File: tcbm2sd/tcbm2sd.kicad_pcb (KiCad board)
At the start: 2 copper layers, 56 x 91 mm, 24 parts, among them J1 TCBM, J2 JTAG, J3 GPIO, J4 AMS1117, J5 SD CARD, J6 ALT_A4_A7, J7 ALT_A6_A7, U1 XC9572XL-VQ64, U2 Arduino Pro Mini, U3 AMS1117-3.3

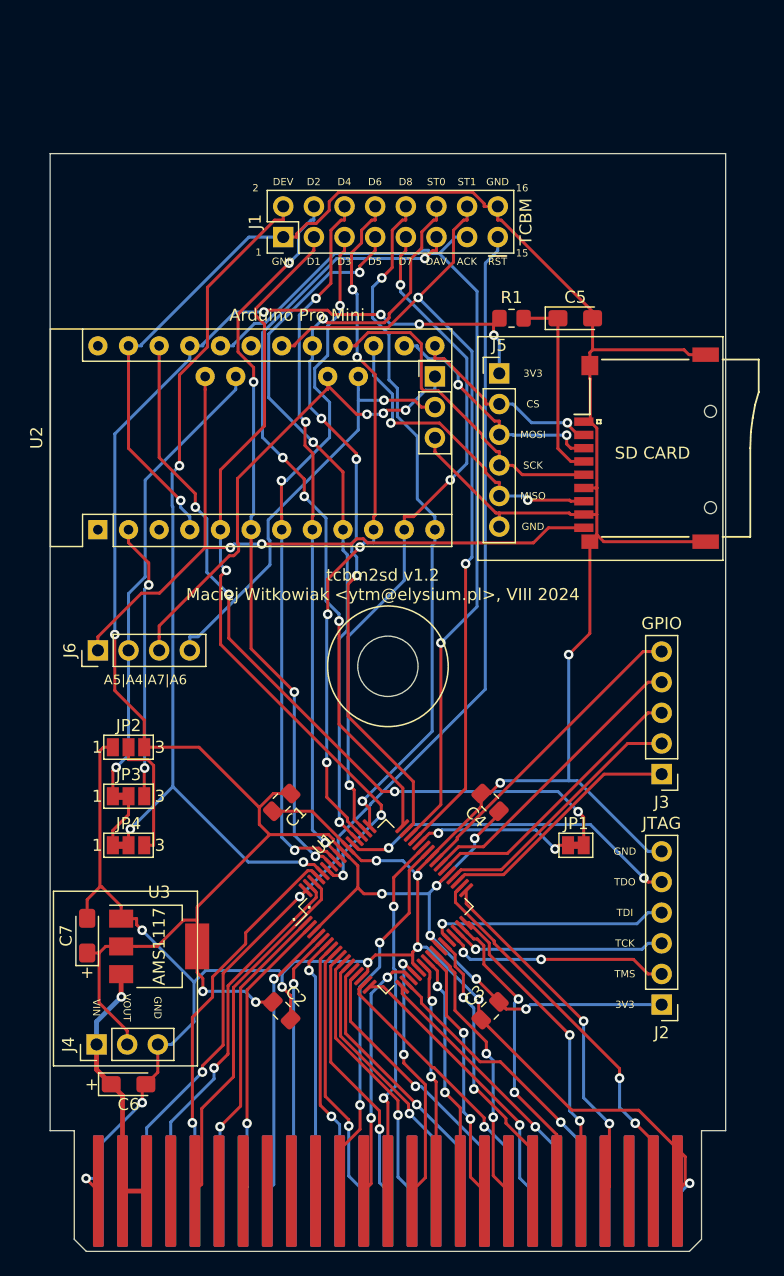
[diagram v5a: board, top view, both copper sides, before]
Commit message: add 32/64K EEPROM with /CS done using two diodes with pullup as AND one more pullup for A15 line connector for remaining Arduino lines with GND connection to short it to disable Arduino on boot
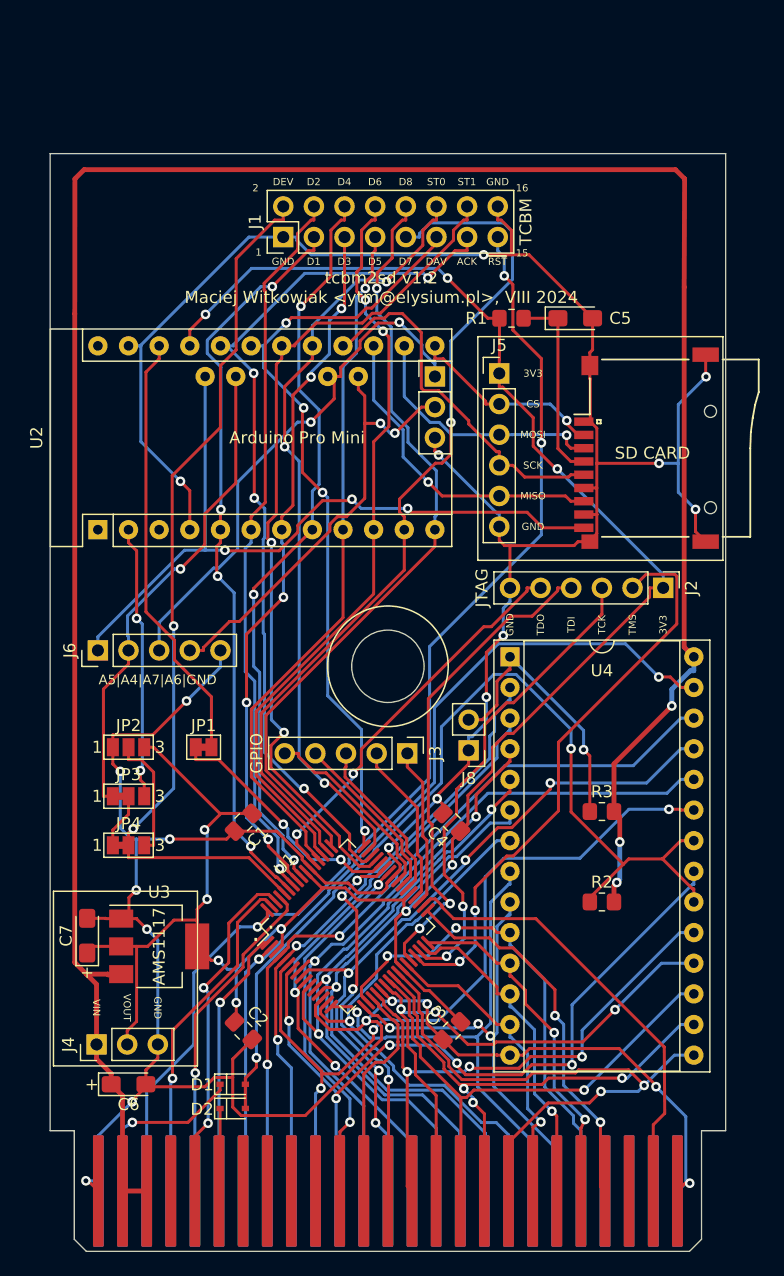
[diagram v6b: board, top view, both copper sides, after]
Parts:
- added D1: 1N4148WS, Diode_SMD:D_SOD-323, F.Cu at (135.6, 136.7)
- added D2: 1N4148WS, Diode_SMD:D_SOD-323, F.Cu at (135.6, 138.7)
- added J8: Conn_01x02, Connector_PinHeader_2.54mm:PinHeader_1x02_P2.54mm_Vertical, F.Cu at (155.2, 109.0)
- added R2: 10K, Resistor_SMD:R_0805_2012Metric_Pad1.20x1.40mm_HandSolder, F.Cu at (166.2, 121.5)
- added R3: 10K, Resistor_SMD:R_0805_2012Metric_Pad1.20x1.40mm_HandSolder, F.Cu at (166.2, 114.0)
- added U4: 27C512, Package_DIP:DIP-28_W15.24mm_Socket, F.Cu at (158.6, 101.2)
- J6: footprint Connector_PinHeader_2.54mm:PinHeader_1x04_P2.54mm_Vertical -> Connector_PinHeader_2.54mm:PinHeader_1x05_P2.54mm_Vertical
- moved J2 34.5 mm to (171.3, 95.5), turned to -90 degrees
- moved JP1 31.9 mm to (133.2, 108.7)
- moved J3 21.2 mm to (150.1, 109.2), turned to -90 degrees
- moved C4 3.58 mm to (153.8, 114.9)
- moved U1 3.58 mm to (145.2, 123.6)
- moved C3 3.58 mm to (153.8, 132.2)
- moved C1 3.58 mm to (136.5, 114.9)
- moved C2 3.58 mm to (136.5, 132.2)
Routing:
- net /VCC: track 21.7 -> 205.3 mm, vias 1 -> 3
- net /~{ROMCS}: track 0.00 -> 81.1 mm, vias 0 -> 2
- net /A14: track 24.2 -> 73.2 mm, vias 1 -> 2
- net /A11: track 21.3 -> 65.9 mm, vias 1 -> 3
- net /A10: track 21.2 -> 63.4 mm, vias 1 -> 5
- net /A13: track 23.0 -> 62.9 mm, vias 1 -> 2
- net /A8: track 21.7 -> 61.5 mm, vias 1 -> 5
- net /A9: track 21.4 -> 60.9 mm
- net /A6: track 22.2 -> 53.6 mm, vias 1 -> 2
- net /TMS: track 18.9 -> 48.0 mm
- net /A12: track 21.9 -> 51.0 mm, vias 1 -> 2
- net Net-(JP1-Pad2): track 64.5 -> 36.0 mm, vias 4 -> 0
- net /D6: track 19.3 -> 47.2 mm, vias 2 -> 3
- net /A7: track 22.0 -> 48.2 mm, vias 1 -> 2
- net /D7: track 21.4 -> 47.6 mm, vias 2 -> 3
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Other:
- board text added: "A5|A4|A7|A6|GND"
- board text added: "JP1: pass computer reset to Arduino JP2: select h/w DEV #9 (1-2) or #8 (2-3) JP3: select s/w DEV from A4 (1-2) or RX (D0) (2-3) JP4: select s/w DEV (1-2) or h/w DEV (2-3) J8: 32K ROM: open J8: 64K ROM: short for low 32K, open for hi 32K"
- board text removed: "A5|A4|A7|A6"
- board text removed: "JP1: pass computer reset to Arduino JP2: select h/w DEV #9 (1-2) or #8 (2-3) JP3: select s/w DEV from A4 (1-2) or RX (D0) (2-3) JP4: select s/w DEV (1-2) or h/w DEV (2-3)"

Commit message: added 32/64K EPROM and its /CS driver: 74HC00+AND gate on diodes+pullup added next/previous buttons removed A4-A7 connector (all pins occupied now) routed A6 to TCBM:16 to sense short to GND (cable attached) central hole back to 5mm
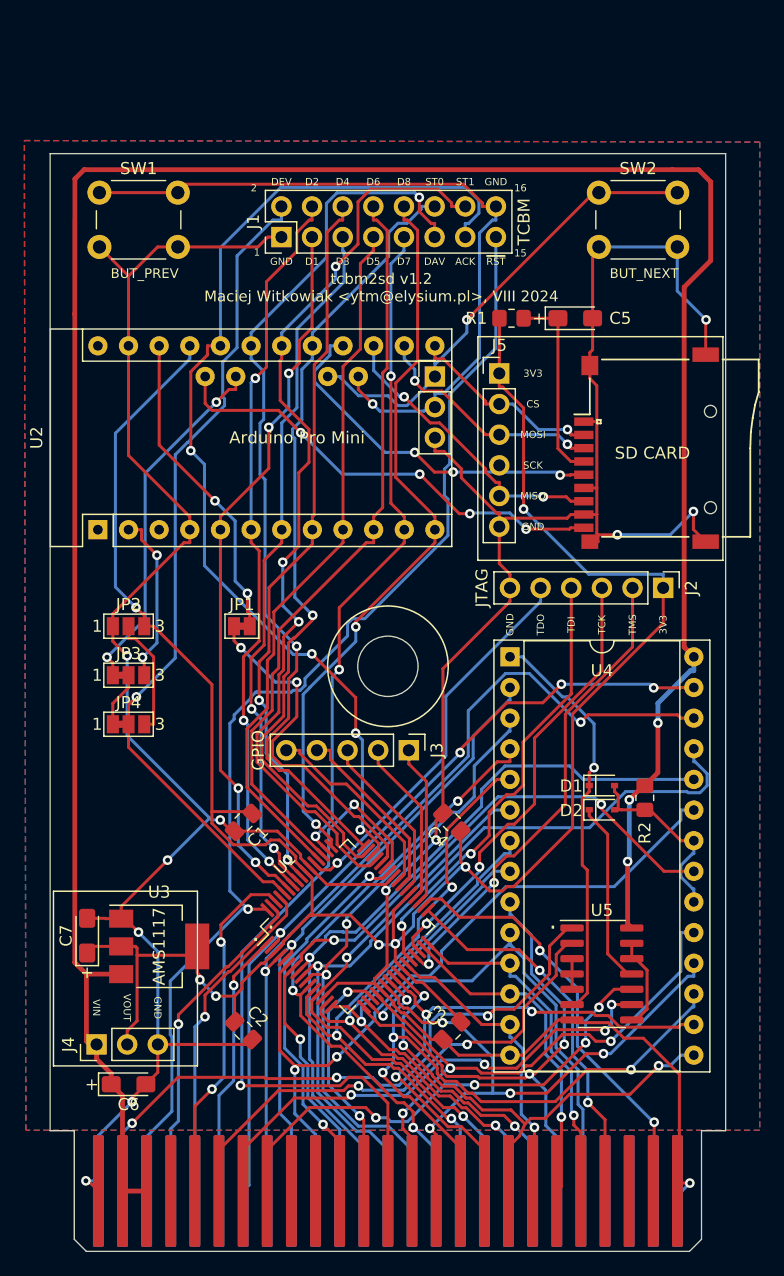
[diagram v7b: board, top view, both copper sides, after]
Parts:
- removed J6: ALT_A4_A7, Connector_PinHeader_2.54mm:PinHeader_1x05_P2.54mm_Vertical
- removed J8: Conn_01x02, Connector_PinHeader_2.54mm:PinHeader_1x02_P2.54mm_Vertical
- removed R3: 10K, Resistor_SMD:R_0805_2012Metric_Pad1.20x1.40mm_HandSolder
- added SW1: BUT_PREV, Button_Switch_THT:SW_PUSH_6mm, F.Cu at (124.6, 62.7)
- added SW2: BUT_NEXT, Button_Switch_THT:SW_PUSH_6mm, F.Cu at (166.0, 62.7)
- added U5: 74HC00, Package_SO:SO-14_3.9x8.65mm_P1.27mm, F.Cu at (166.2, 127.5)
- moved D2 39.4 mm to (166.2, 113.9)
- moved D1 39.4 mm to (166.2, 111.9)
- moved JP1 10.5 mm to (136.4, 98.7)
- moved JP2 10.0 mm to (127.0, 98.7)
- moved JP3 10.0 mm to (127.0, 102.7)
- moved JP4 10.0 mm to (127.0, 106.8)
- moved R2 9.34 mm to (169.8, 112.9), turned to 90 degrees
- moved J3 0.28 mm to (150.2, 109.0)
- moved J1 0.15 mm to (139.7, 66.4)
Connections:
- net /ALT_A4 renamed Net-(JP3-Pad1)
- D1 pad 1: /C1LO -> /ROM_A15
- D2 pad 1: /C1HI -> Net-(D2-Pad1)
- J1 pad 16: GND -> /ALT_A6
- U4 pad 1: Net-(J8-Pad2) -> /ROM_A15
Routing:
- net /~{ROMCS}: track 81.1 -> 15.4 mm, vias 2 -> 0
- net /C2LO: track 0.00 -> 38.8 mm, vias 0 -> 4
- net /C2HI: track 0.00 -> 37.9 mm, vias 0 -> 4
- net /C1LO: track 15.0 -> 52.4 mm, vias 1 -> 3
- net /ROM_A15: track 0.00 -> 33.5 mm, vias 0 -> 1
- net /C1HI: track 6.76 -> 38.3 mm, vias 0 -> 2
- net GND: track 326.9 -> 299.5 mm, vias 22 -> 12
- net /SD_CD: track 61.9 -> 38.0 mm, vias 3 -> 4
- net /ALT_A6: track 37.6 -> 61.4 mm, vias 2 -> 1
- net Net-(J8-Pad2): track 22.9 -> 0.00 mm, vias 1 -> 0
- net /BA: track 31.8 -> 54.7 mm, vias 4 -> 2
- net +3V3: track 180.8 -> 198.7 mm, vias 10 -> 7
- net /DIO7: track 72.6 -> 55.2 mm, vias 1 -> 3
- net Net-(D2-Pad1): track 0.00 -> 14.9 mm
- net /ACK: track 73.4 -> 87.6 mm
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- added copper zone on B.Cu, net GND
- added copper zone on F.Cu, net GND
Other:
- board text added: "Important: Connect TCBM cable GND to both pins 1 AND 16"
- board text added: "JP1: pass computer reset to Arduino JP2: select h/w DEV #9 (1-2) or #8 (2-3) JP3: select s/w DEV from A4 (1-2) or RX (D0) (2-3) JP4: select s/w DEV (1-2) or h/w DEV (2-3)"
- board text removed: "A5|A4|A7|A6|GND"
- board text removed: "JP1: pass computer reset to Arduino JP2: select h/w DEV #9 (1-2) or #8 (2-3) JP3: select s/w DEV from A4 (1-2) or RX (D0) (2-3) JP4: select s/w DEV (1-2) or h/w DEV (2-3) J8: 32K ROM: open J8: 64K ROM: short for low 32K, open for hi 32K"

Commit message: production files
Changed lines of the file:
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@@
     (fp_line (start -1.6 -0.4) (end -1.6 0.8) (layer "F.Fab") (width 0.1))
     (fp_line (start -1.2 -0.8) (end -1.6 -0.4) (layer "F.Fab") (width 0.1))
-    (pad "1" smd roundrect (at -1.4375 0) (size 1.575 1.35) (layers "F.Cu" "F.Paste" "F.Mask") (roundrect_rratio 0.185185)
+    (pad "1" smd roundrect (at -1.4375 0) (size 1.575 1.35) (layers "F.Cu" "F.Paste" "F.Mask") (roundrect_rratio 0.1851851852)
       (net 27 "/VCC") (pintype "passive"))
-    (pad "2" smd roundrect (at 1.4375 0) (size 1.575 1.35) (layers "F.Cu" "F.Paste" "F.Mask") (roundrect_rratio 0.185185)
+    (pad "2" smd roundrect (at 1.4375 0) (size 1.575 1.35) (layers "F.Cu" "F.Paste" "F.Mask") (roundrect_rratio 0.1851851852)
       (net 17 "GND") (pintype "passive"))
     (model "${KICAD6_3DMODEL_DIR}/Capacitor_Tantalum_SMD.3dshapes/CP_EIA-3216-12_Kemet-S.wrl"
@@
     (fp_line (start 1.6 -0.8) (end -1.2 -0.8) (layer "F.Fab") (width 0.1))
     (fp_line (start -1.2 -0.8) (end -1.6 -0.4) (layer "F.Fab") (width 0.1))
-    (pad "1" smd roundrect (at -1.4375 0 90) (size 1.575 1.35) (layers "F.Cu" "F.Paste" "F.Mask") (roundrect_rratio 0.185185)
+    (pad "1" smd roundrect (at -1.4375 0 90) (size 1.575 1.35) (layers "F.Cu" "F.Paste" "F.Mask") (roundrect_rratio 0.1851851852)
       (net 45 "+3V3") (pintype "passive"))
-    (pad "2" smd roundrect (at 1.4375 0 90) (size 1.575 1.35) (layers "F.Cu" "F.Paste" "F.Mask") (roundrect_rratio 0.185185)
+    (pad "2" smd roundrect (at 1.4375 0 90) (size 1.575 1.35) (layers "F.Cu" "F.Paste" "F.Mask") (roundrect_rratio 0.1851851852)
       (net 17 "GND") (pintype "passive"))
     (model "${KICAD6_3DMODEL_DIR}/Capacitor_Tantalum_SMD.3dshapes/CP_EIA-3216-12_Kemet-S.wrl"
@@
     (fp_line (start 1 0.625) (end -1 0.625) (layer "F.Fab") (width 0.1))
     (fp_line (start 1 -0.625) (end 1 0.625) (layer "F.Fab") (width 0.1))
-    (pad "1" smd roundrect (at -1 0 90) (size 1.2 1.4) (layers "F.Cu" "F.Paste" "F.Mask") (roundrect_rratio 0.208333)
+    (pad "1" smd roundrect (at -1 0 90) (size 1.2 1.4) (layers "F.Cu" "F.Paste" "F.Mask") (roundrect_rratio 0.2083333333)
       (net 87 "/~{ROMCS}") (pintype "passive"))
-    (pad "2" smd roundrect (at 1 0 90) (size 1.2 1.4) (layers "F.Cu" "F.Paste" "F.Mask") (roundrect_rratio 0.208333)
+    (pad "2" smd roundrect (at 1 0 90) (size 1.2 1.4) (layers "F.Cu" "F.Paste" "F.Mask") (roundrect_rratio 0.2083333333)
       (net 27 "/VCC") (pintype "passive"))
     (model "${KICAD6_3DMODEL_DIR}/Resistor_SMD.3dshapes/R_0805_2012Metric.wrl"
@@
     (fp_line (start -1.6 -0.4) (end -1.6 0.8) (layer "F.Fab") (width 0.1))
     (fp_line (start 1.6 0.8) (end 1.6 -0.8) (layer "F.Fab") (width 0.1))
-    (pad "1" smd roundrect (at -1.4375 0) (size 1.575 1.35) (layers "F.Cu" "F.Paste" "F.Mask") (roundrect_rratio 0.185185)
+    (pad "1" smd roundrect (at -1.4375 0) (size 1.575 1.35) (layers "F.Cu" "F.Paste" "F.Mask") (roundrect_rratio 0.1851851852)
       (net 77 "Net-(C5-Pad1)") (pintype "passive"))
-    (pad "2" smd roundrect (at 1.4375 0) (size 1.575 1.35) (layers "F.Cu" "F.Paste" "F.Mask") (roundrect_rratio 0.185185)
+    (pad "2" smd roundrect (at 1.4375 0) (size 1.575 1.35) (layers "F.Cu" "F.Paste" "F.Mask") (roundrect_rratio 0.1851851852)
       (net 17 "GND") (pintype "passive"))
     (model "${KICAD6_3DMODEL_DIR}/Capacitor_Tantalum_SMD.3dshapes/CP_EIA-3216-12_Kemet-S.wrl"
@@
     (fp_line (start 1 0.625) (end -1 0.625) (layer "F.Fab") (width 0.1))
     (fp_line (start -1 0.625) (end -1 -0.625) (layer "F.Fab") (width 0.1))
-    (pad "1" smd roundrect (at -1 0 180) (size 1.2 1.4) (layers "F.Cu" "F.Paste" "F.Mask") (roundrect_rratio 0.208333)
+    (pad "1" smd roundrect (at -1 0 180) (size 1.2 1.4) (layers "F.Cu" "F.Paste" "F.Mask") (roundrect_rratio 0.2083333333)
       (net 77 "Net-(C5-Pad1)") (pintype "passive"))
-    (pad "2" smd roundrect (at 1 0 180) (size 1.2 1.4) (layers "F.Cu" "F.Paste" "F.Mask") (roundrect_rratio 0.208333)
+    (pad "2" smd roundrect (at 1 0 180) (size 1.2 1.4) (layers "F.Cu" "F.Paste" "F.Mask") (roundrect_rratio 0.2083333333)
       (net 45 "+3V3") (pintype "passive"))
     (model "${KICAD6_3DMODEL_DIR}/Resistor_SMD.3dshapes/R_0805_2012Metric.wrl"
